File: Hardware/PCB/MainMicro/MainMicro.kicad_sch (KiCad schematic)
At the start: 61 parts, among them J1 Conn_02x05_Odd_Even, J10 Conn_01x03_Male, J11 Conn_01x05_Male, J12 Conn_01x05_Male, J2 USB_B_Mini, J3 Barrel_Jack, J4 Conn_01x05_Male, J5 Conn_01x06_Male, J6 Conn_01x06_Male, J7 Conn_01x03_Male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

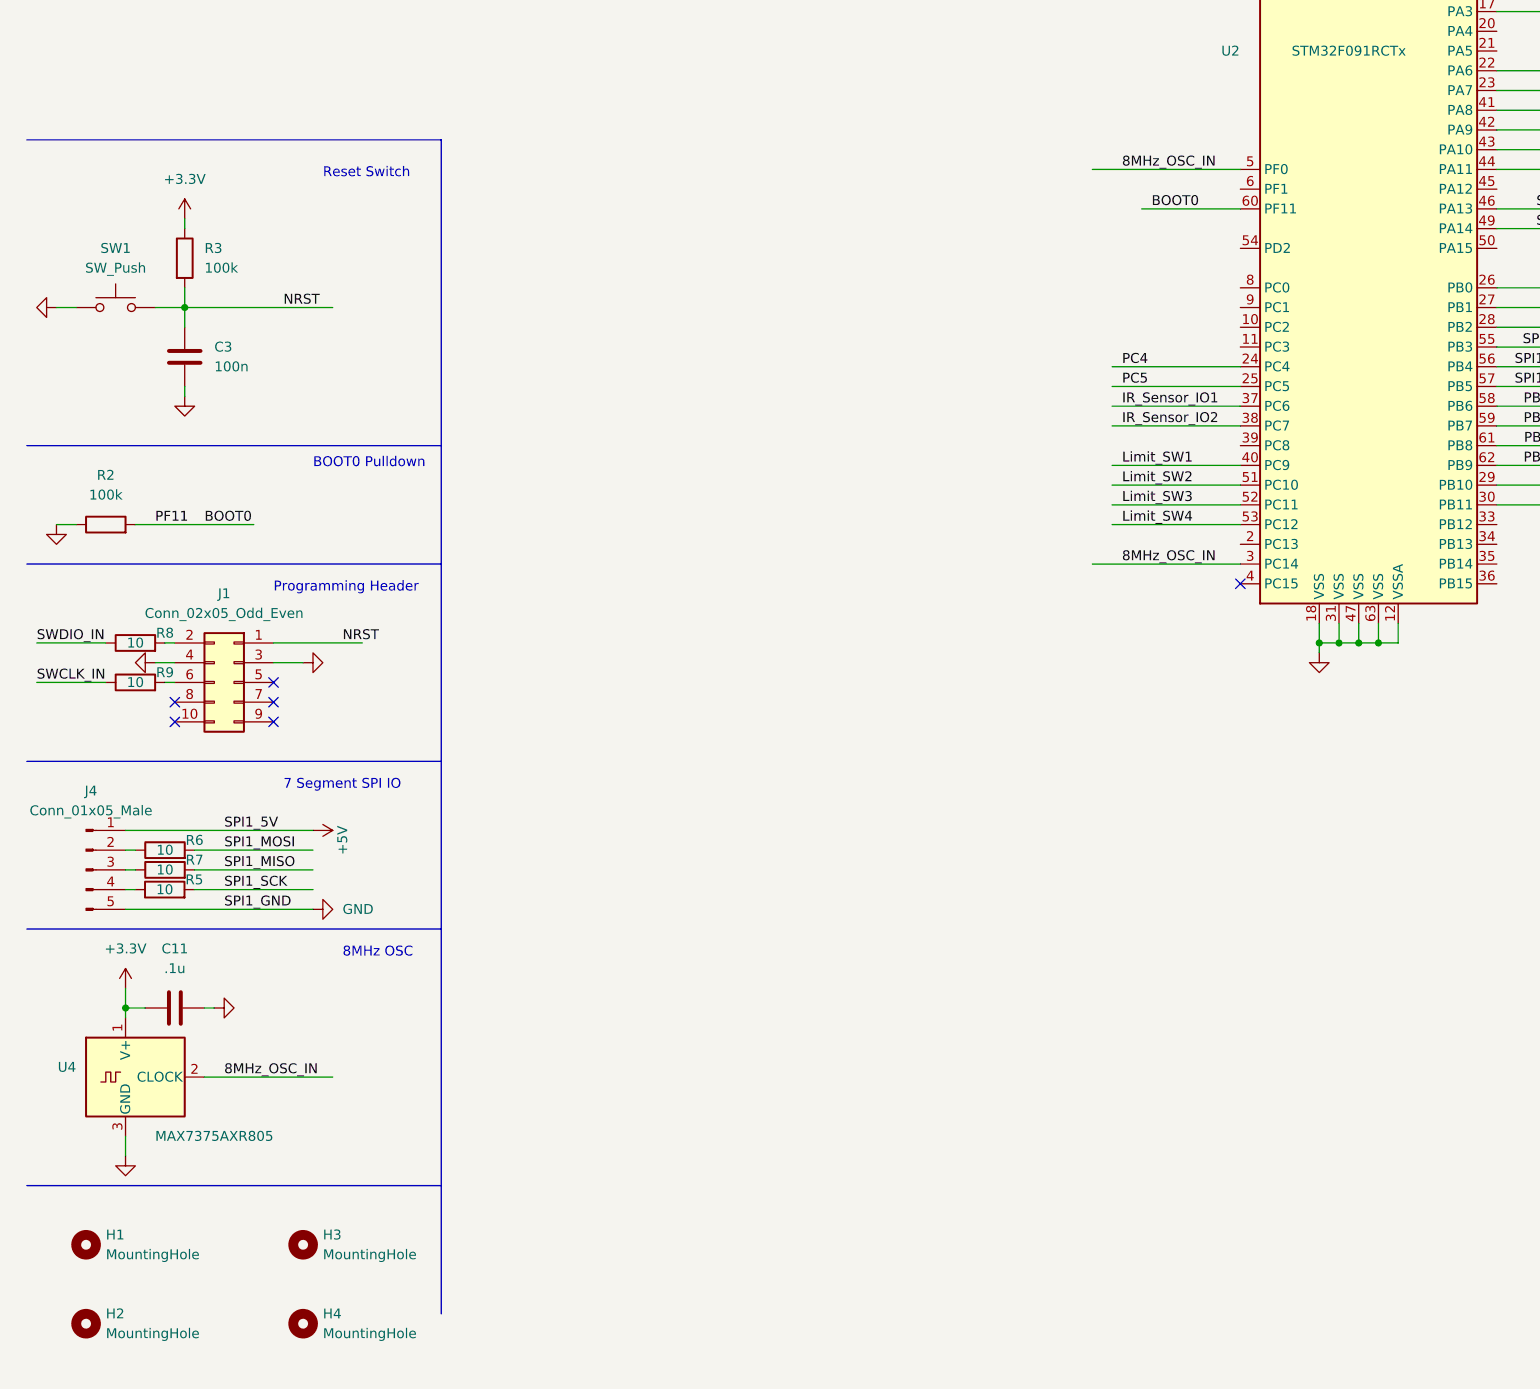
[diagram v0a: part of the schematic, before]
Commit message: Added Logic translation for SPI
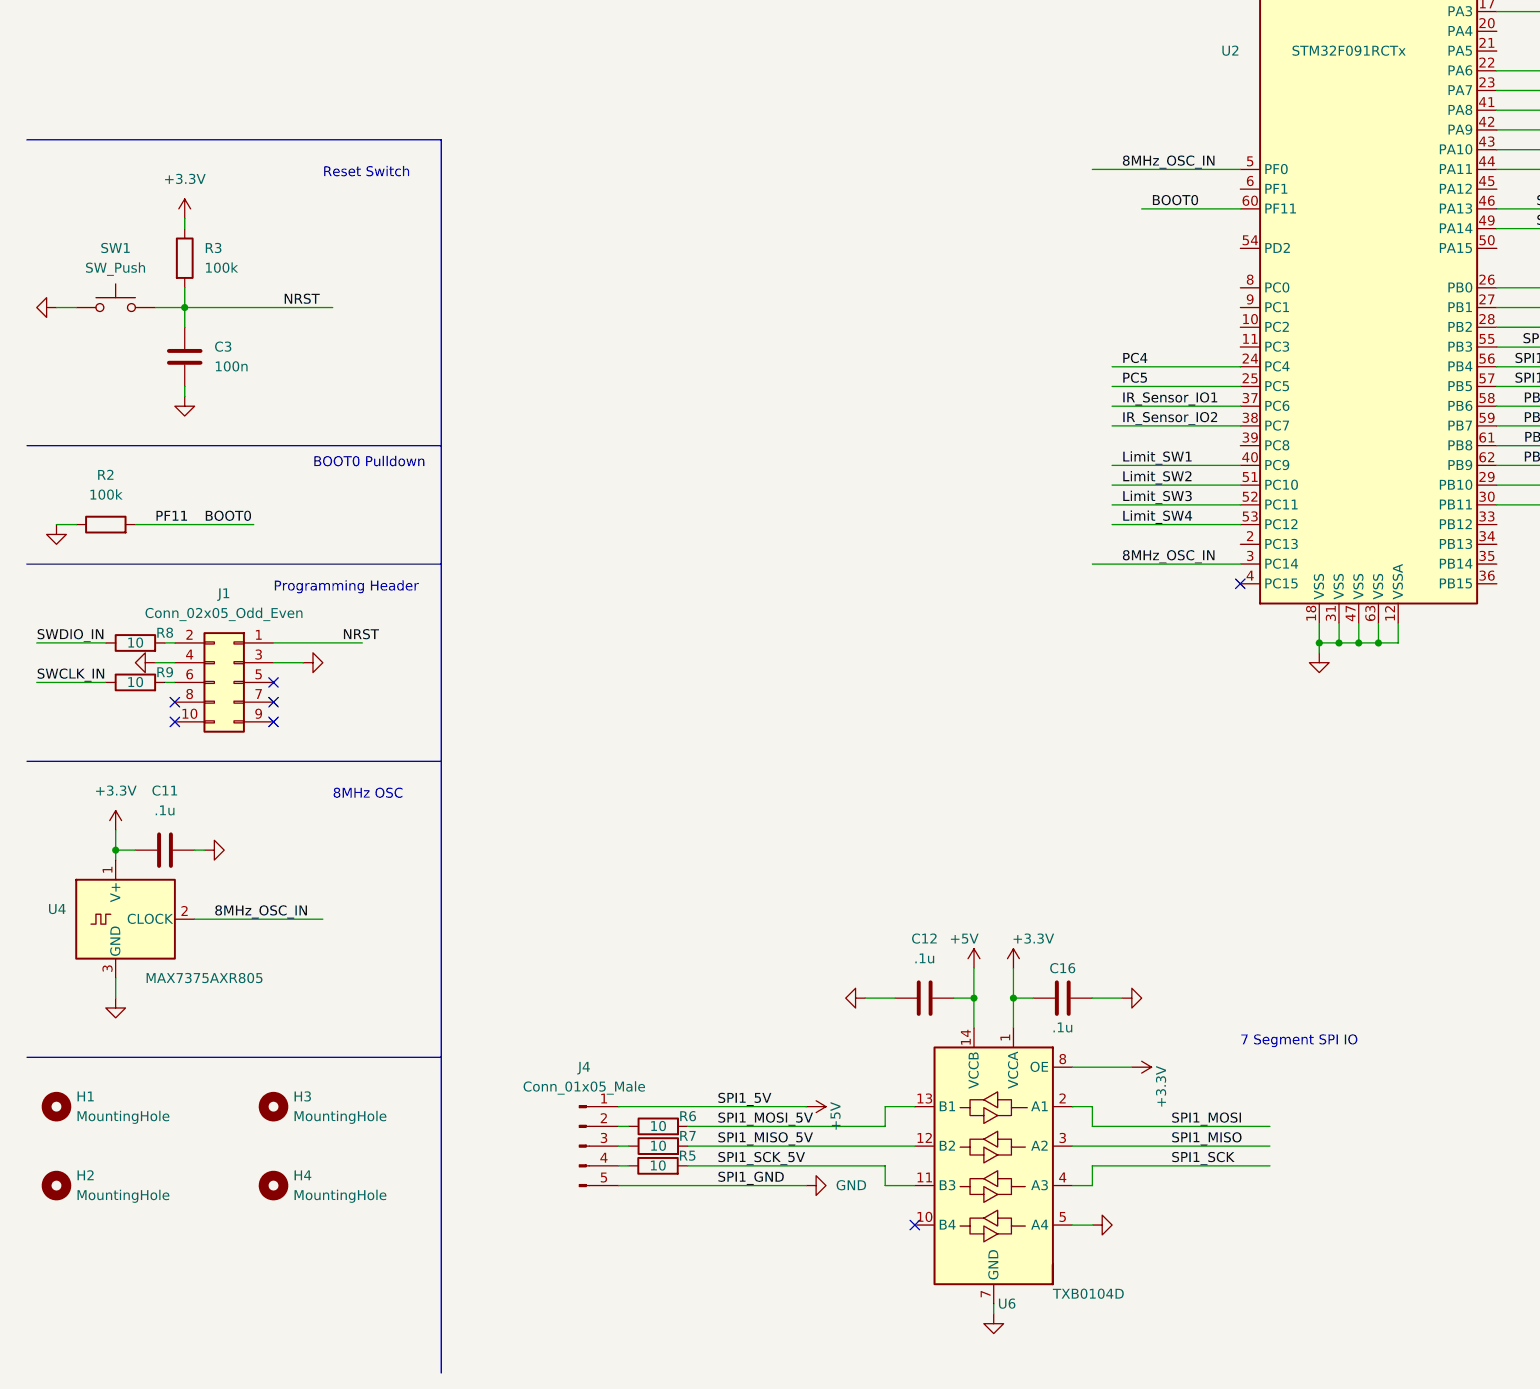
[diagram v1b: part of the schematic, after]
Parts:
- added C12, C16: .1u, Capacitor_SMD:C_0805_2012Metric_Pad1.18x1.45mm_HandSolder, symbol Device:C
- added U6: TXB0104D, Package_SO:SOIC-14_3.9x8.7mm_P1.27mm, symbol Logic_LevelTranslator:TXB0104D
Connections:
- net +3V3: now also C16.2, U6.1 (VCCA), U6.8 (OE)
- net +5V: now also C12.1, U6.14 (VCCB)
- net GND: now also C12.2, C16.1, U6.5 (A4), U6.7 (GND)
- net SPI1_MISO: now also U6.3 (A2); no longer R7.2
- net SPI1_MOSI: now also U6.2 (A1); no longer R6.2
- net SPI1_SCK: now also U6.4 (A3); no longer R5.2
- new net SPI1_MISO_5V: R7.2, U6.12 (B2)
- new net SPI1_MOSI_5V: R6.2, U6.13 (B1)
- new net SPI1_SCK_5V: R5.2, U6.11 (B3)
- no-connect marks 21 -> 22
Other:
- moved on the sheet: C11, H1, H2, H3, H4, J4, R5, R6, R7, U4

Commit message: Please don't break
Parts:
- removed U3: FT232RL, Package_SO:SSOP-28_5.3x10.2mm_P0.65mm, symbol Interface_USB:FT232RL
- added C17: 100n, Capacitor_SMD:C_0805_2012Metric_Pad1.18x1.45mm_HandSolder, symbol Device:C
- added J13: Conn_01x04_Female, Connector_JST:JST_EH_B4B-EH-A_1x04_P2.50mm_Vertical, symbol Connector:Conn_01x04_Female
- added J14: Conn_01x02_Male, Connector_JST:JST_EH_B2B-EH-A_1x02_P2.50mm_Vertical, symbol Connector:Conn_01x02_Male
- added R22: 100k, Resistor_SMD:R_0805_2012Metric_Pad1.20x1.40mm_HandSolder, symbol Device:R
- added R23: 10, Resistor_SMD:R_0805_2012Metric_Pad1.20x1.40mm_HandSolder, symbol Device:R
- added U3: FT231XS, Package_SO:SSOP-20_3.9x8.7mm_P0.635mm, symbol Interface_USB:FT231XS
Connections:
- net +3V3: now also R22.1
- net GND: now also C17.2, J14.2 (Pin_2), U3.16 (GND), U3.6 (GND)
- net NRST: now also U3.14 (~{RESET})
- net USART2_CTS: now also J13.1 (Pin_1), U3.9 (~{CTS})
- net USART2_RTS: now also J13.2 (Pin_2), U3.2 (~{RTS})
- net USART2_RX: now also J13.3 (Pin_3), U3.4 (RXD)
- net USART2_TX: now also J13.4 (Pin_4), U3.20 (TXD)
- net USB_D+: now also U3.11 (USBDP)
- net USB_D-: now also U3.12 (USBDM)
- net VUSB 5V: now also U3.3 (VCCIO)
- net PA6 renamed PA6_GPI
- net PA6_GPI: now also R23.2
- net SPI1_MISO renamed SPI1_LATCH
- net SPI1_MISO_5V renamed SPI1_LATCH_5V
- new net: U3.13 (3V3OUT), U3.15 (VCC)
- new net: C17.1, J14.1 (Pin_1), R22.2, R23.1
- no-connect marks 22 -> 18
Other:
- note added: "Big Red Button"
- moved on the sheet: J2

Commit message: Commit for PCB final
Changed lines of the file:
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@@
     (stroke (width 0) (type default) (color 0 0 0 0))
   )
-  (polyline (pts (xy 66.04 212.09) (xy 190.5 212.09))
+  (polyline (pts (xy 67.31 212.09) (xy 191.77 212.09))
     (stroke (width 0) (type default) (color 0 0 0 0))
   )
@@
     (stroke (width 0) (type default) (color 0 0 0 0))
   )
-  (polyline (pts (xy 190.5 212.09) (xy 190.5 284.48))
+  (polyline (pts (xy 191.77 212.09) (xy 190.5 284.48))
     (stroke (width 0) (type default) (color 0 0 0 0))
   )

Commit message: Generated Main Micro Gerber Files
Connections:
- net 8MHz_OSC_IN: no longer U2.3 (PC14)
- no-connect marks 18 -> 35
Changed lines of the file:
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@@
   (no_connect (at 44.45 200.66))
   (no_connect (at 127 265.43))
+  (no_connect (at 201.93 175.26))
+  (no_connect (at 201.93 177.8))
+  (no_connect (at 201.93 180.34))
+  (no_connect (at 201.93 182.88))
+  (no_connect (at 201.93 139.7))
+  (no_connect (at 201.93 132.08))
+  (no_connect (at 201.93 111.76))
+  (no_connect (at 201.93 114.3))
+  (no_connect (at 168.91 180.34))
+  (no_connect (at 168.91 177.8))
+  (no_connect (at 168.91 165.1))
+  (no_connect (at 168.91 152.4))
+  (no_connect (at 168.91 149.86))
+  (no_connect (at 168.91 147.32))
+  (no_connect (at 168.91 144.78))
+  (no_connect (at 168.91 139.7))
+  (no_connect (at 168.91 132.08))
   (no_connect (at 388.62 40.64))
   (no_connect (at 314.96 50.8))
@@
     (stroke (width 0) (type default) (color 0 0 0 0))
   )
-  (wire (pts (xy 149.86 180.34) (xy 168.91 180.34))
-    (stroke (width 0) (type default) (color 0 0 0 0))
-  )
   (wire (pts (xy 336.55 182.88) (xy 336.55 167.64))
     (stroke (width 0) (type default) (color 0 0 0 0))
@@
     (effects (font (size 1.27 1.27)) (justify left bottom))
   )
-  (label "8MHz_OSC_IN" (at 153.67 180.34 0)
-    (effects (font (size 1.27 1.27)) (justify left bottom))
-  )

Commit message: Post joe
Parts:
- removed D2: BAT60JFILM, Diode_SMD:D_SOD-323, symbol Diode:BAT60A
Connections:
- net BJ5V is gone; now on net +5V: J3.1
- net +3V3: now also U5.2 (DIR)
- net PB6_GPO: no longer names the net of U2.58 (PB6)
- net PB6_GPO: no longer U5.2 (DIR)
- no-connect marks 35 -> 36
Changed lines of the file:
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@@
   (no_connect (at 314.96 50.8))
   (no_connect (at 314.96 71.12))
+  (no_connect (at 201.93 160.02))
   (no_connect (at 350.52 138.43))
   (no_connect (at 350.52 140.97))
@@
     (stroke (width 0) (type default) (color 0 0 0 0))
   )
-  (wire (pts (xy 311.15 118.11) (xy 325.12 118.11))
-    (stroke (width 0) (type default) (color 0 0 0 0))
-  )
   (wire (pts (xy 353.06 30.48) (xy 335.28 30.48))
     (stroke (width 0) (type default) (color 0 0 0 0))
@@
     (stroke (width 0) (type default) (color 0 0 0 0))
   )
-  (wire (pts (xy 43.18 72.39) (xy 48.26 72.39))
-    (stroke (width 0) (type default) (color 0 0 0 0))
-  )
   (polyline (pts (xy 12.7 99.06) (xy 87.63 99.06))
     (stroke (width 0) (type default) (color 0 0 0 0))
@@
     (stroke (width 0) (type default) (color 0 0 0 0))
   )
-  (wire (pts (xy 33.02 72.39) (xy 35.56 72.39))
+  (wire (pts (xy 33.02 72.39) (xy 48.26 72.39))
     (stroke (width 0) (type default) (color 0 0 0 0))
   )
@@
     (stroke (width 0) (type default) (color 0 0 0 0))
   )
-  (wire (pts (xy 201.93 160.02) (xy 214.63 160.02))
-    (stroke (width 0) (type default) (color 0 0 0 0))
-  )
   (wire (pts (xy 330.2 19.05) (xy 330.2 33.02))
     (stroke (width 0) (type default) (color 0 0 0 0))
@@
     (stroke (width 0) (type default) (color 0 0 0 0))
   )
+  (wire (pts (xy 321.31 118.11) (xy 325.12 118.11))
+    (stroke (width 0) (type default) (color 0 0 0 0))
+  )
   (wire (pts (xy 20.32 30.48) (xy 20.32 35.56))
     (stroke (width 0) (type default) (color 0 0 0 0))
@@
     (stroke (width 0) (type default) (color 0 0 0 0))
   )
+  (wire (pts (xy 321.31 116.84) (xy 321.31 118.11))
+    (stroke (width 0) (type default) (color 0 0 0 0))
+  )
   (wire (pts (xy 214.63 152.4) (xy 201.93 152.4))
     (stroke (width 0) (type default) (color 0 0 0 0))
@@
     (effects (font (size 1.27 1.27)) (justify right bottom))
   )
-  (label "PB6_GPO" (at 311.15 118.11 0)
-    (effects (font (size 1.27 1.27)) (justify left bottom))
-  )
   (label "NRST" (at 355.6 55.88 0)
     (effects (font (size 1.27 1.27)) (justify left bottom))
@@
     (effects (font (size 1.27 1.27)) (justify left bottom))
   )
-  (label "PB6_GPO" (at 213.36 160.02 180)
-    (effects (font (size 1.27 1.27)) (justify right bottom))
-  )
   (label "PA8_GPO" (at 208.28 121.92 0)
     (effects (font (size 1.27 1.27)) (justify left bottom))
@@
     (pin "2")
   )
+  (symbol (lib_id "power:+3.3V") (at 321.31 116.84 90) (unit 1)
+    (in_bom yes) (on_board yes)
+    (property "Reference" "#PWR?" (id 0) (at 325.12 116.84 0)
+      (effects (font (size 1.27 1.27)) hide)
+    )
+    (property "Value" "+3.3V" (id 1) (at 317.5 118.11 0))
+    (property "Footprint" "" (id 2) (at 321.31 116.84 0)
+      (effects (font (size 1.27 1.27)) hide)
+    )
+    (property "Datasheet" "" (id 3) (at 321.31 116.84 0)
+      (effects (font (size 1.27 1.27)) hide)
+    )
+    (pin "1")
+  )
   (symbol (lib_id "Device:R") (at 351.79 224.79 90) (unit 1)
     (in_bom yes) (on_board yes)
@@
     (pin "2")
   )
-  (symbol (lib_id "Diode:BAT60A") (at 39.37 72.39 180) (unit 1)
-    (in_bom yes) (on_board yes)
-    (property "Reference" "D2" (id 0) (at 39.37 66.8782 0))
-    (property "Value" "BAT60JFILM" (id 1) (at 39.37 69.1896 0))
-    (property "Footprint" "Diode_SMD:D_SOD-323" (id 2) (at 39.37 67.945 0)
-      (effects (font (size 1.27 1.27)) hide)
-    )
-    (property "Datasheet" "https://www.infineon.com/dgdl/Infineon-BAT60ASERIES-DS-v01_01-en.pdf?fileId=db3a304313d846880113def70c9304a9" (id 3) (at 39.37 72.39 0)
-      (effects (font (size 1.27 1.27)) hide)
-    )
-    (pin "1")
-    (pin "2")
-  )
   (symbol (lib_id "power:GND") (at 367.03 125.73 270) (unit 1)
     (in_bom yes) (on_board yes) (fields_autoplaced)
@@
       (reference "#PWR0150") (unit 1) (value "GND") (footprint "")
     )
+    (path "/117b2dd3-5681-4de4-bc26-dffa8c801a74"
+      (reference "#PWR?") (unit 1) (value "+3.3V") (footprint "")
+    )
     (path "/a6ed9d0d-ba92-45ee-b109-ace861dda2d9"
       (reference "C1") (unit 1) (value "22u") (footprint "Capacitor_SMD:C_0805_2012Metric_Pad1.18x1.45mm_HandSolder")
@@
       (reference "D1") (unit 1) (value "LED") (footprint "LED_SMD:LED_0603_1608Metric_Pad1.05x0.95mm_HandSolder")
     )
-    (path "/a94ddf33-d801-4471-8443-414b44e33bb3"
-      (reference "D2") (unit 1) (value "BAT60JFILM") (footprint "Diode_SMD:D_SOD-323")
-    )
     (path "/3d1b0f7d-cb60-480d-80e4-0ca62d862def"
